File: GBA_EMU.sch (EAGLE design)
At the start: 95 parts, among them J1 USB-MINIB-5PIN, J2 AVR_SPI, Q1 MOSFET-PCHANNEL, SW1 LEFT, SW2 RIGHT, SW3 PWR_SWITCH, U2 FT230X, U4 LM4875, U5 Mic5365-2.8Y, U7 AZV321, X2 HEADPHONE

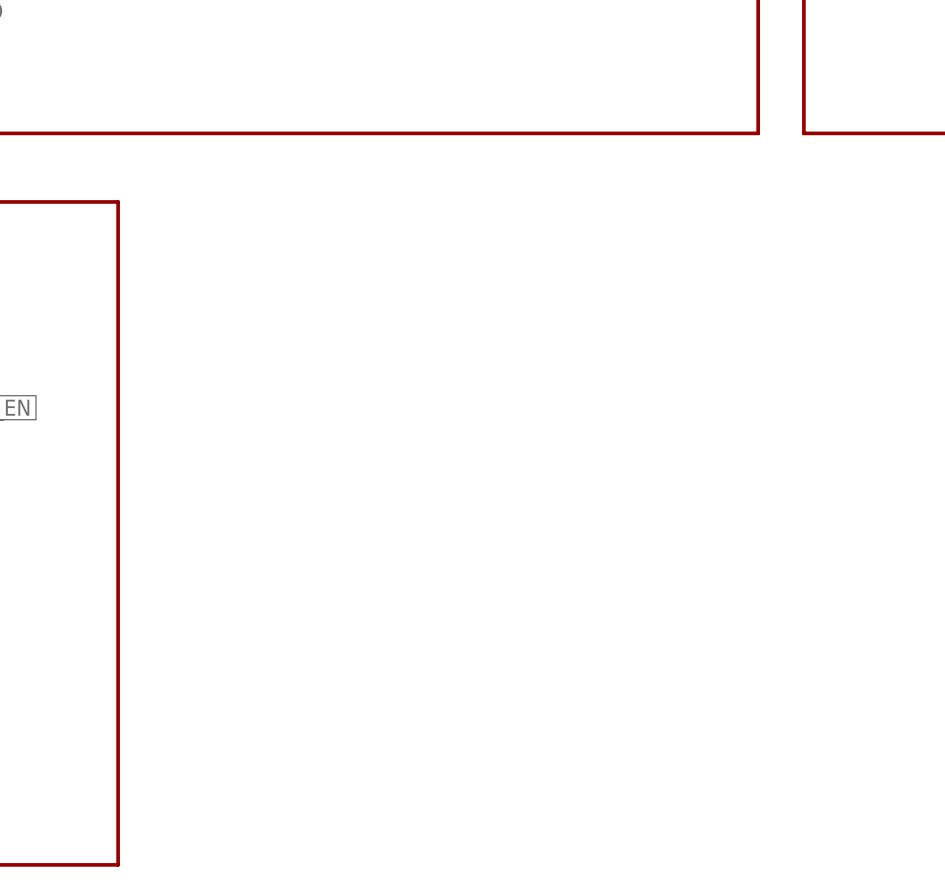
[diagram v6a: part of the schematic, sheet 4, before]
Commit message: added the HDMI plug :/
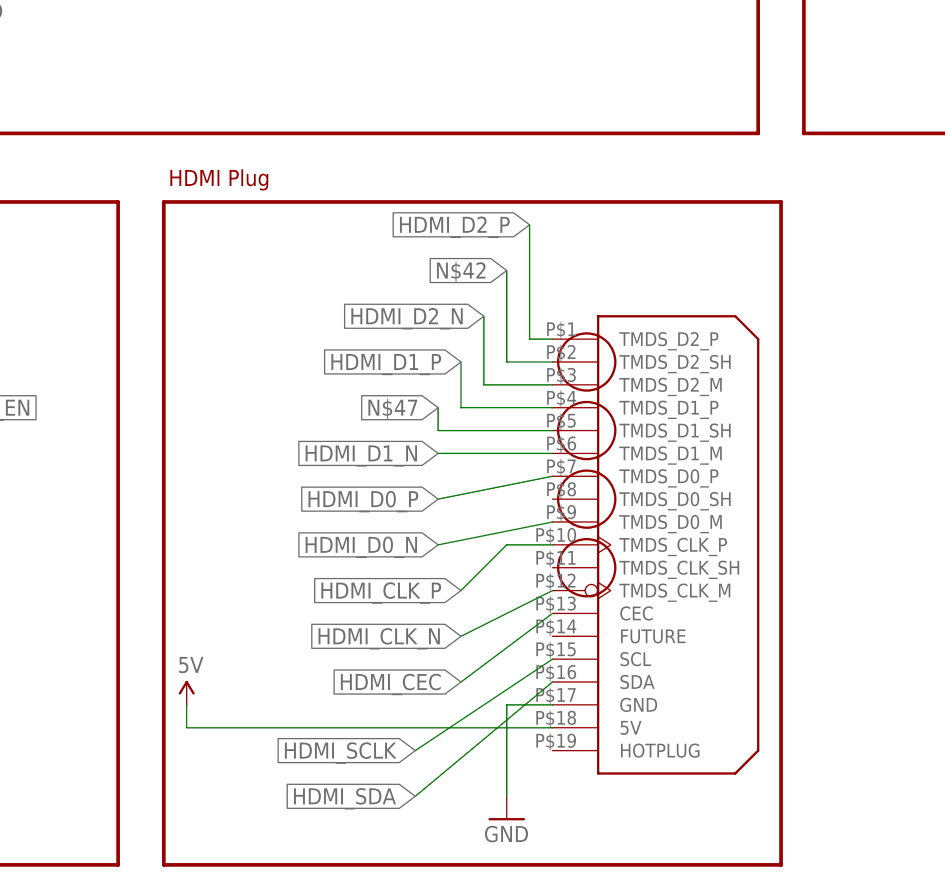
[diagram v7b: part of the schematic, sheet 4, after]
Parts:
- added U$8: HDMI_A_RECPT, custom:HDMI_A_RECPT
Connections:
- new net HDMI_CEC: PCB1.171/HDMI_CEC, U$8.CEC
- new net HDMI_CLK_N: PCB1.111/HDMI_CK_N*, U$8.TMDS_CLK_M
- new net HDMI_CLK_P: PCB1.113/HDMI_CK_P*, U$8.TMDS_CLK_P
- new net HDMI_D0_N: PCB1.117/HDMI_D0_N*, U$8.TMDS_D0_M
- new net HDMI_D0_P: PCB1.119/HDMI_D0_P*, U$8.TMDS_D0_P
- new net HDMI_D1_N: PCB1.123/HDMI_D1_N*, U$8.TMDS_D1_M
- new net HDMI_D1_P: PCB1.125/HDMI_D1_P*, U$8.TMDS_D1_P
- new net HDMI_D2_N: PCB1.129/HDMI_D2_N*, U$8.TMDS_D2_M
- new net HDMI_D2_P: PCB1.131/HDMI_D2_P*, U$8.TMDS_D2_P
- new net HDMI_SCLK: PCB1.175/HDMI_SCL, U$8.SCL
- new net HDMI_SDA: PCB1.173/HDMI_SDA, U$8.SDA
- new net N$42: U$8.TMDS_D2_SH
- new net N$47: U$8.TMDS_D1_SH
- net 5V: now also U$8.5V
- net GND: now also U$8.GND
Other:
- note added: "HDMI Plug"
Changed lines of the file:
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@@
 <class number="0" name="default" width="0" drill="0">
+</class>
+<class number="1" name="diff pairs" width="0.4064" drill="0">
 </class>
 </classes>
@@
 <part name="T1" library="custom" deviceset="TRANSISTOR_PNP_DRIVER" device="SC59-BEC" technology="MUN2111T1"/>
 <part name="R12" library="SparkFun-Resistors" deviceset="1KOHM-1/10W-1%(0603)" device="" value="1K"/>
+<part name="U$8" library="custom" deviceset="HDMI_A_RECPT" device=""/>
+<part name="SUPPLY34" library="SparkFun-Aesthetics" deviceset="5V" device=""/>
+<part name="GND46" library="SparkFun-Aesthetics" deviceset="GND" device=""/>
 </parts>
 <sheets>
@@
 </segment>
 </net>
+<net name="HDMI_D1_N" class="1">
+<segment>
+<pinref part="PCB1" gate="G$1" pin="123/HDMI_D1_N*"/>
+<wire x1="33.02" y1="0" x2="-5.08" y2="0" width="0.1524" layer="91"/>
+<label x="-5.08" y="0" size="1.778" layer="95" rot="R180" xref="yes"/>
+</segment>
+</net>
+<net name="HDMI_D1_P" class="1">
+<segment>
+<pinref part="PCB1" gate="G$1" pin="125/HDMI_D1_P*"/>
+<wire x1="33.02" y1="-2.54" x2="20.32" y2="-2.54" width="0.1524" layer="91"/>
+<label x="20.32" y="-2.54" size="1.778" layer="95" rot="R180" xref="yes"/>
+</segment>
+</net>
+<net name="HDMI_D0_N" class="1">
+<segment>
+<pinref part="PCB1" gate="G$1" pin="117/HDMI_D0_N*"/>
+<wire x1="33.02" y1="7.62" x2="-5.08" y2="7.62" width="0.1524" layer="91"/>
+<label x="-5.08" y="7.62" size="1.778" layer="95" rot="R180" xref="yes"/>
+</segment>
+</net>
+<net name="HDMI_D0_P" class="1">
+<segment>
+<pinref part="PCB1" gate="G$1" pin="119/HDMI_D0_P*"/>
+<wire x1="33.02" y1="5.08" x2="20.32" y2="5.08" width="0.1524" layer="91"/>
+<label x="20.32" y="5.08" size="1.778" layer="95" rot="R180" xref="yes"/>
+</segment>
+</net>
+<net name="HDMI_CLK_P" class="1">
+<segment>
+<pinref part="PCB1" gate="G$1" pin="113/HDMI_CK_P*"/>
+<wire x1="33.02" y1="12.7" x2="20.32" y2="12.7" width="0.1524" layer="91"/>
+<label x="20.32" y="12.7" size="1.778" layer="95" rot="R180" xref="yes"/>
+</segment>
+</net>
+<net name="HDMI_CLK_N" class="1">
+<segment>
+<pinref part="PCB1" gate="G$1" pin="111/HDMI_CK_N*"/>
+<wire x1="33.02" y1="15.24" x2="-5.08" y2="15.24" width="0.1524" layer="91"/>
+<label x="-5.08" y="15.24" size="1.778" layer="95" rot="R180" xref="yes"/>
+</segment>
+</net>
+<net name="HDMI_D2_N" class="1">
+<segment>
+<pinref part="PCB1" gate="G$1" pin="129/HDMI_D2_N*"/>
+<wire x1="33.02" y1="-7.62" x2="-5.08" y2="-7.62" width="0.1524" layer="91"/>
+<label x="-5.08" y="-7.62" size="1.778" layer="95" rot="R180" xref="yes"/>
+</segment>
+</net>
+<net name="HDMI_D2_P" class="1">
+<segment>
+<pinref part="PCB1" gate="G$1" pin="131/HDMI_D2_P*"/>
+<wire x1="33.02" y1="-10.16" x2="20.32" y2="-10.16" width="0.1524" layer="91"/>
+<label x="20.32" y="-10.16" size="1.778" layer="95" rot="R180" xref="yes"/>
+</segment>
+</net>
+<net name="HDMI_CEC" class="1">
+<segment>
+<pinref part="PCB1" gate="G$1" pin="171/HDMI_CEC"/>
+<wire x1="38.1" y1="-60.96" x2="10.16" y2="-60.96" width="0.1524" layer="91"/>
+<label x="5.08" y="-55.88" size="1.778" layer="95" rot="R180" xref="yes"/>
+<wire x1="10.16" y1="-60.96" x2="5.08" y2="-55.88" width="0.1524" layer="91"/>
+</segment>
+</net>
+<net name="HDMI_SDA" class="0">
+<segment>
+<pinref part="PCB1" gate="G$1" pin="173/HDMI_SDA"/>
+<wire x1="38.1" y1="-63.5" x2="7.62" y2="-63.5" width="0.1524" layer="91"/>
+<wire x1="7.62" y1="-63.5" x2="5.08" y2="-60.96" width="0.1524" layer="91"/>
+<label x="5.08" y="-60.96" size="1.778" layer="95" rot="R180" xref="yes"/>
+</segment>
+</net>
+<net name="HDMI_SCLK" class="0">
+<segment>
+<pinref part="PCB1" gate="G$1" pin="175/HDMI_SCL"/>
+<wire x1="38.1" y1="-66.04" x2="5.08" y2="-66.04" width="0.1524" layer="91"/>
+<label x="5.08" y="-66.04" size="1.778" layer="95" rot="R180" xref="yes"/>
+</segment>
+</net>
 </nets>
 </sheet>
@@
 <wire x1="259.08" y1="76.2" x2="259.08" y2="157.48" width="0.4064" layer="94"/>
 <text x="132.08" y="160.02" size="1.778" layer="94">Battery Controller</text>
-<wire x1="0" y1="68.58" x2="53.34" y2="68.58" width="0.4064" layer="94"/>
-<wire x1="53.34" y1="68.58" x2="53.34" y2="-5.08" width="0.4064" layer="94"/>
 <wire x1="53.34" y1="-5.08" x2="0" y2="-5.08" width="0.4064" layer="94"/>
 <wire x1="0" y1="-5.08" x2="0" y2="68.58" width="0.4064" layer="94"/>
 <text x="0.508" y="70.358" size="1.778" layer="94">FAN</text>
+<wire x1="0" y1="68.58" x2="53.34" y2="68.58" width="0.4064" layer="94"/>
+<wire x1="58.42" y1="68.58" x2="127" y2="68.58" width="0.4064" layer="94"/>
+<wire x1="53.34" y1="68.58" x2="53.34" y2="-5.08" width="0.4064" layer="94"/>
+<wire x1="58.42" y1="68.58" x2="58.42" y2="-5.08" width="0.4064" layer="94"/>
+<wire x1="127" y1="68.58" x2="127" y2="-5.08" width="0.4064" layer="94"/>
+<wire x1="58.42" y1="-5.08" x2="127" y2="-5.08" width="0.4064" layer="94"/>
+<text x="58.928" y="70.358" size="1.778" layer="94">HDMI Plug</text>
 </plain>
 <instances>
@@
 <instance part="T1" gate="G$1" x="22.86" y="30.48" rot="R180"/>
 <instance part="R12" gate="G$1" x="33.02" y="38.1" rot="R90"/>
+<instance part="U$8" gate="G$1" x="109.22" y="38.1"/>
+<instance part="SUPPLY34" gate="G$1" x="60.96" y="12.7"/>
+<instance part="GND46" gate="1" x="96.52" y="0"/>
 </instances>
 <busses>
@@
 <wire x1="20.32" y1="25.4" x2="20.32" y2="15.24" width="0.1524" layer="91"/>
 </segment>
+<segment>
+<pinref part="U$8" gate="G$1" pin="GND"/>
+<wire x1="101.6" y1="12.7" x2="96.52" y2="12.7" width="0.1524" layer="91"/>
+<wire x1="96.52" y1="12.7" x2="96.52" y2="2.54" width="0.1524" layer="91"/>
+<pinref part="GND46" gate="1" pin="GND"/>
+</segment>
 </net>
 <net name="5V" class="0">
@@
 <pinref part="FAN" gate="G$1" pin="2"/>
 <wire x1="22.86" y1="40.64" x2="17.78" y2="40.64" width="0.1524" layer="91"/>
+</segment>
+<segment>
+<pinref part="U$8" gate="G$1" pin="5V"/>
+<wire x1="101.6" y1="10.16" x2="60.96" y2="10.16" width="0.1524" layer="91"/>
+<wire x1="60.96" y1="10.16" x2="60.96" y2="12.7" width="0.1524" layer="91"/>
+<pinref part="SUPPLY34" gate="G$1" pin="5V"/>
 </segment>
 </net>
@@
 </segment>
 </net>
+<net name="HDMI_D2_P" class="1">
+<segment>
+<pinref part="U$8" gate="G$1" pin="TMDS_D2_P"/>
+<wire x1="101.6" y1="53.34" x2="99.06" y2="53.34" width="0.1524" layer="91"/>
+<wire x1="99.06" y1="53.34" x2="99.06" y2="66.04" width="0.1524" layer="91"/>
+<label x="99.06" y="66.04" size="1.778" layer="95" rot="R180" xref="yes"/>
+</segment>
+</net>
+<net name="N$42" class="0">
+<segment>
+<pinref part="U$8" gate="G$1" pin="TMDS_D2_SH"/>
+<wire x1="101.6" y1="50.8" x2="96.52" y2="50.8" width="0.1524" layer="91"/>
+<wire x1="96.52" y1="50.8" x2="96.52" y2="60.96" width="0.1524" layer="91"/>
+<label x="96.52" y="60.96" size="1.778" layer="95" rot="R180" xref="yes"/>
+</segment>
+</net>
+<net name="HDMI_D2_N" class="1">
+<segment>
+<pinref part="U$8" gate="G$1" pin="TMDS_D2_M"/>
+<wire x1="101.6" y1="48.26" x2="93.98" y2="48.26" width="0.1524" layer="91"/>
+<wire x1="93.98" y1="48.26" x2="93.98" y2="55.88" width="0.1524" layer="91"/>
+<label x="93.98" y="55.88" size="1.778" layer="95" rot="R180" xref="yes"/>
+</segment>
+</net>
+<net name="HDMI_D1_P" class="1">
+<segment>
+<pinref part="U$8" gate="G$1" pin="TMDS_D1_P"/>
+<wire x1="101.6" y1="45.72" x2="91.44" y2="45.72" width="0.1524" layer="91"/>
+<wire x1="91.44" y1="45.72" x2="91.44" y2="50.8" width="0.1524" layer="91"/>
+<label x="91.44" y="50.8" size="1.778" layer="95" rot="R180" xref="yes"/>
+</segment>
+</net>
+<net name="N$47" class="0">
+<segment>
+<pinref part="U$8" gate="G$1" pin="TMDS_D1_SH"/>
+<wire x1="101.6" y1="43.18" x2="88.9" y2="43.18" width="0.1524" layer="91"/>
+<wire x1="88.9" y1="43.18" x2="88.9" y2="45.72" width="0.1524" layer="91"/>
+<label x="88.9" y="45.72" size="1.778" layer="95" rot="R180" xref="yes"/>
+</segment>
+</net>
+<net name="HDMI_D1_N" class="1">
+<segment>
+<pinref part="U$8" gate="G$1" pin="TMDS_D1_M"/>
+<wire x1="101.6" y1="40.64" x2="88.9" y2="40.64" width="0.1524" layer="91"/>
+<label x="88.9" y="40.64" size="1.778" layer="95" rot="R180" xref="yes"/>
+</segment>
+</net>
+<net name="HDMI_D0_P" class="1">
+<segment>
+<pinref part="U$8" gate="G$1" pin="TMDS_D0_P"/>
+<wire x1="101.6" y1="38.1" x2="88.9" y2="35.56" width="0.1524" layer="91"/>
+<label x="88.9" y="35.56" size="1.778" layer="95" rot="R180" xref="yes"/>
+</segment>
+</net>
+<net name="HDMI_D0_N" class="1">
+<segment>
+<pinref part="U$8" gate="G$1" pin="TMDS_D0_M"/>
+<wire x1="101.6" y1="33.02" x2="88.9" y2="30.48" width="0.1524" layer="91"/>
+<label x="88.9" y="30.48" size="1.778" layer="95" rot="R180" xref="yes"/>
+</segment>
+</net>
+<net name="HDMI_CLK_P" class="1">
+<segment>
+<pinref part="U$8" gate="G$1" pin="TMDS_CLK_P"/>
+<wire x1="101.6" y1="30.48" x2="96.52" y2="30.48" width="0.1524" layer="91"/>
+<wire x1="96.52" y1="30.48" x2="91.44" y2="25.4" width="0.1524" layer="91"/>
+<label x="91.44" y="25.4" size="1.778" layer="95" rot="R180" xref="yes"/>
+</segment>
+</net>
+<net name="HDMI_CLK_N" class="1">
+<segment>
+<pinref part="U$8" gate="G$1" pin="TMDS_CLK_M"/>
+<wire x1="101.6" y1="25.4" x2="91.44" y2="20.32" width="0.1524" layer="91"/>
+<label x="91.44" y="20.32" size="1.778" layer="95" rot="R180" xref="yes"/>
+</segment>
+</net>
+<net name="HDMI_SCLK" class="0">
+<segment>
+<pinref part="U$8" gate="G$1" pin="SCL"/>
+<wire x1="101.6" y1="17.78" x2="86.36" y2="7.62" width="0.1524" layer="91"/>
+<label x="86.36" y="7.62" size="1.778" layer="95" rot="R180" xref="yes"/>
+</segment>
+</net>
+<net name="HDMI_SDA" class="0">
+<segment>
+<pinref part="U$8" gate="G$1" pin="SDA"/>
+<wire x1="101.6" y1="15.24" x2="86.36" y2="2.54" width="0.1524" layer="91"/>
+<label x="86.36" y="2.54" size="1.778" layer="95" rot="R180" xref="yes"/>
+</segment>
+</net>
+<net name="HDMI_CEC" class="1">
+<segment>
+<pinref part="U$8" gate="G$1" pin="CEC"/>
+<wire x1="101.6" y1="22.86" x2="91.44" y2="15.24" width="0.1524" layer="91"/>
+<label x="91.44" y="15.24" size="1.778" layer="95" rot="R180" xref="yes"/>
+</segment>
+</net>

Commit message: Added power generation sheet
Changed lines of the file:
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@@
 <part name="SUPPLY34" library="SparkFun-Aesthetics" deviceset="5V" device=""/>
 <part name="GND46" library="SparkFun-Aesthetics" deviceset="GND" device=""/>
+<part name="FRAME5" library="frames" deviceset="A4L-LOC" device=""/>
 </parts>
 <sheets>
@@
 </nets>
 </sheet>
+<sheet>
+<description>Power Generation and management</description>
+<plain>
+</plain>
+<instances>
+<instance part="FRAME5" gate="G$1" x="0" y="0"/>
+</instances>
+<busses>
+</busses>
+<nets>
+</nets>
+</sheet>
